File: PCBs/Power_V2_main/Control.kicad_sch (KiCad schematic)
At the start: 24 parts, among them IC1 W25Q16JVUXIQ_TR, J7 USB_C_Receptacle_USB2.0_16P, U2 ESP32-S3, U3 USBLC6-2SC6, Y1 7M40000010

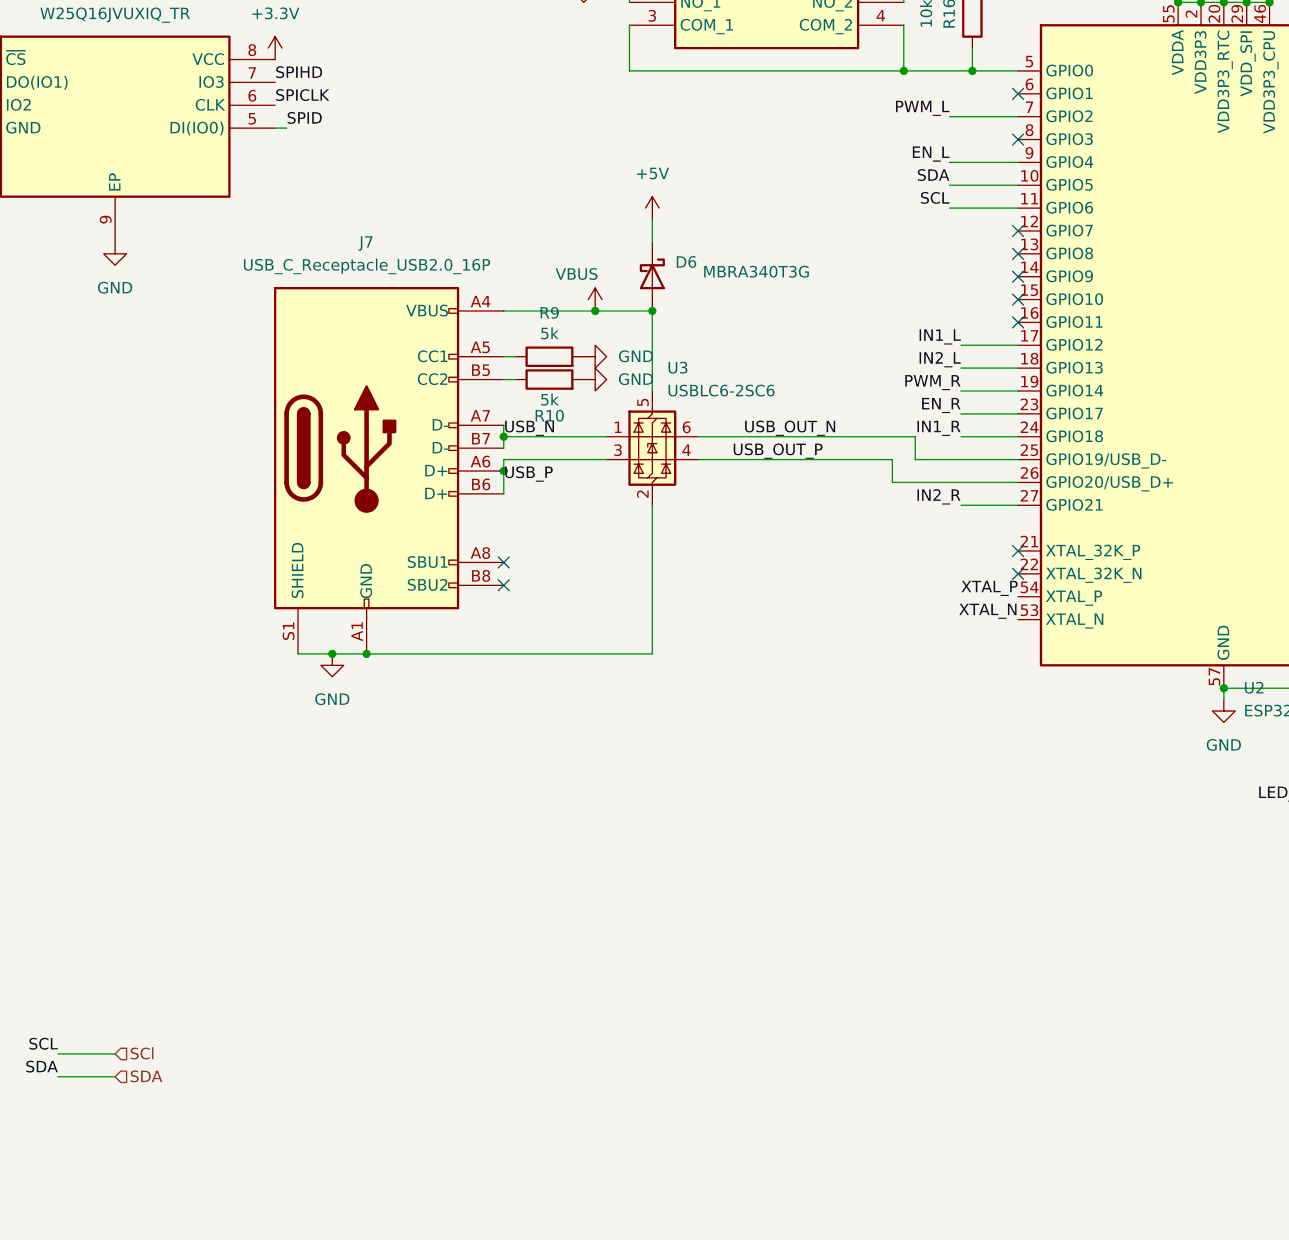
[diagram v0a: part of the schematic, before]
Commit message: shortened main board and secondary
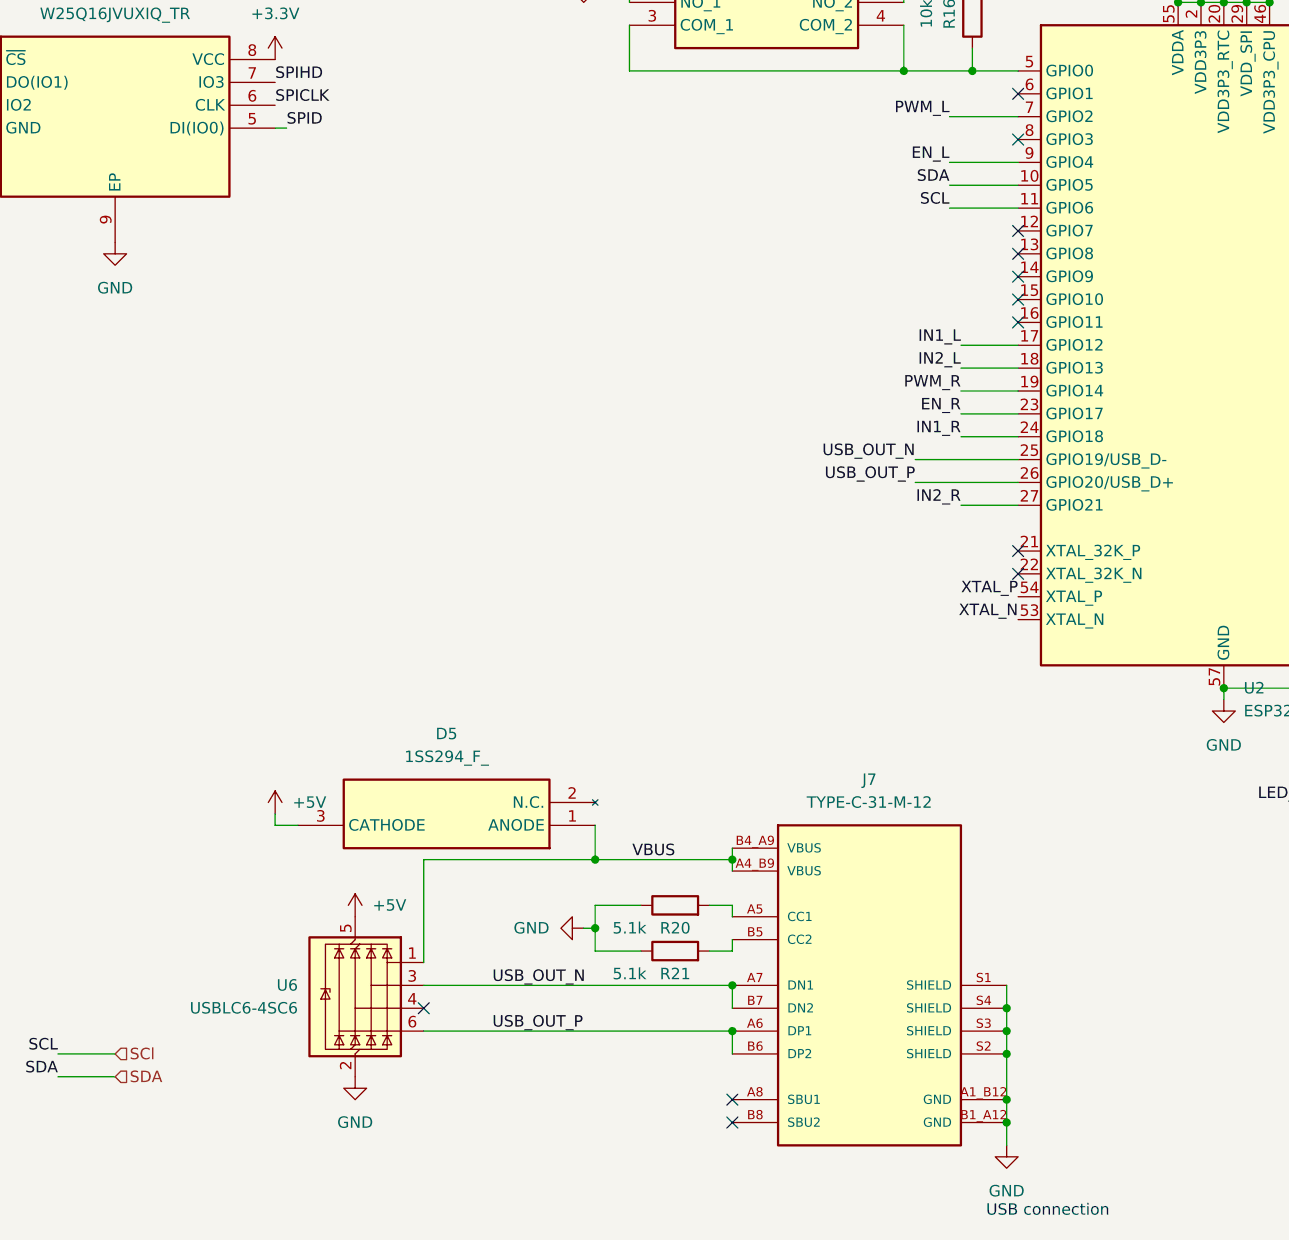
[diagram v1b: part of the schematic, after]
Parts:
- removed D6: MBRA340T3G, Diode_SMD:D_SMA, symbol Device:D_Schottky
- removed J7: USB_C_Receptacle_USB2.0_16P, IPRL_footprints:TYPE-C-31-M-12, symbol Connector:USB_C_Receptacle_USB2.0_16P
- removed R10, R9: 5k, Resistor_SMD:R_0805_2012Metric, symbol Device:R
- removed U3: USBLC6-2SC6, Package_TO_SOT_SMD:SOT-23-6, symbol Power_Protection:USBLC6-2SC6
- added D5: 1SS294_F_, iprl_footprint:SOT95P260X140-3N, symbol 1SS294_F_:1SS294_F_
- added J7: TYPE-C-31-M-12, iprl_footprints:TYPE-C-31-M-12, symbol TYPE-C-31-M-12:TYPE-C-31-M-12
- added R20, R21: 5.1k, Resistor_SMD:R_0805_2012Metric, symbol Device:R
- added U6: USBLC6-4SC6, Package_TO_SOT_SMD:SOT-23-6, symbol Power_Protection:USBLC6-4SC6
- BOOT1: footprint IPRL_footprints:PTS645SK43SMTR92LFS -> iprl_footprints:PTS645SK43SMTR92LFS
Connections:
- net +5V: now also D5.3 (CATHODE), U6.5 (VBUS)
- net GND: now also J7.A1_B12 (GND), J7.B1_A12 (GND), J7.S1 (SHIELD), J7.S2 (SHIELD), J7.S3 (SHIELD), J7.S4 (SHIELD), R20.1, R21.1, U6.2 (GND)
- net USB_OUT_N: now also J7.A7 (DN1), J7.B7 (DN2), U6.3 (I/O2)
- net USB_OUT_P: now also J7.A6 (DP1), J7.B6 (DP2), U6.6 (I/O4)
- net VBUS: now also D5.1 (ANODE), J7.A4_B9 (VBUS), J7.B4_A9 (VBUS), U6.1 (I/O1)
- new net: J7.A5 (CC1), R20.2
- new net: J7.B5 (CC2), R21.2
- no-connect marks 28 -> 29
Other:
- note added: "USB connection"

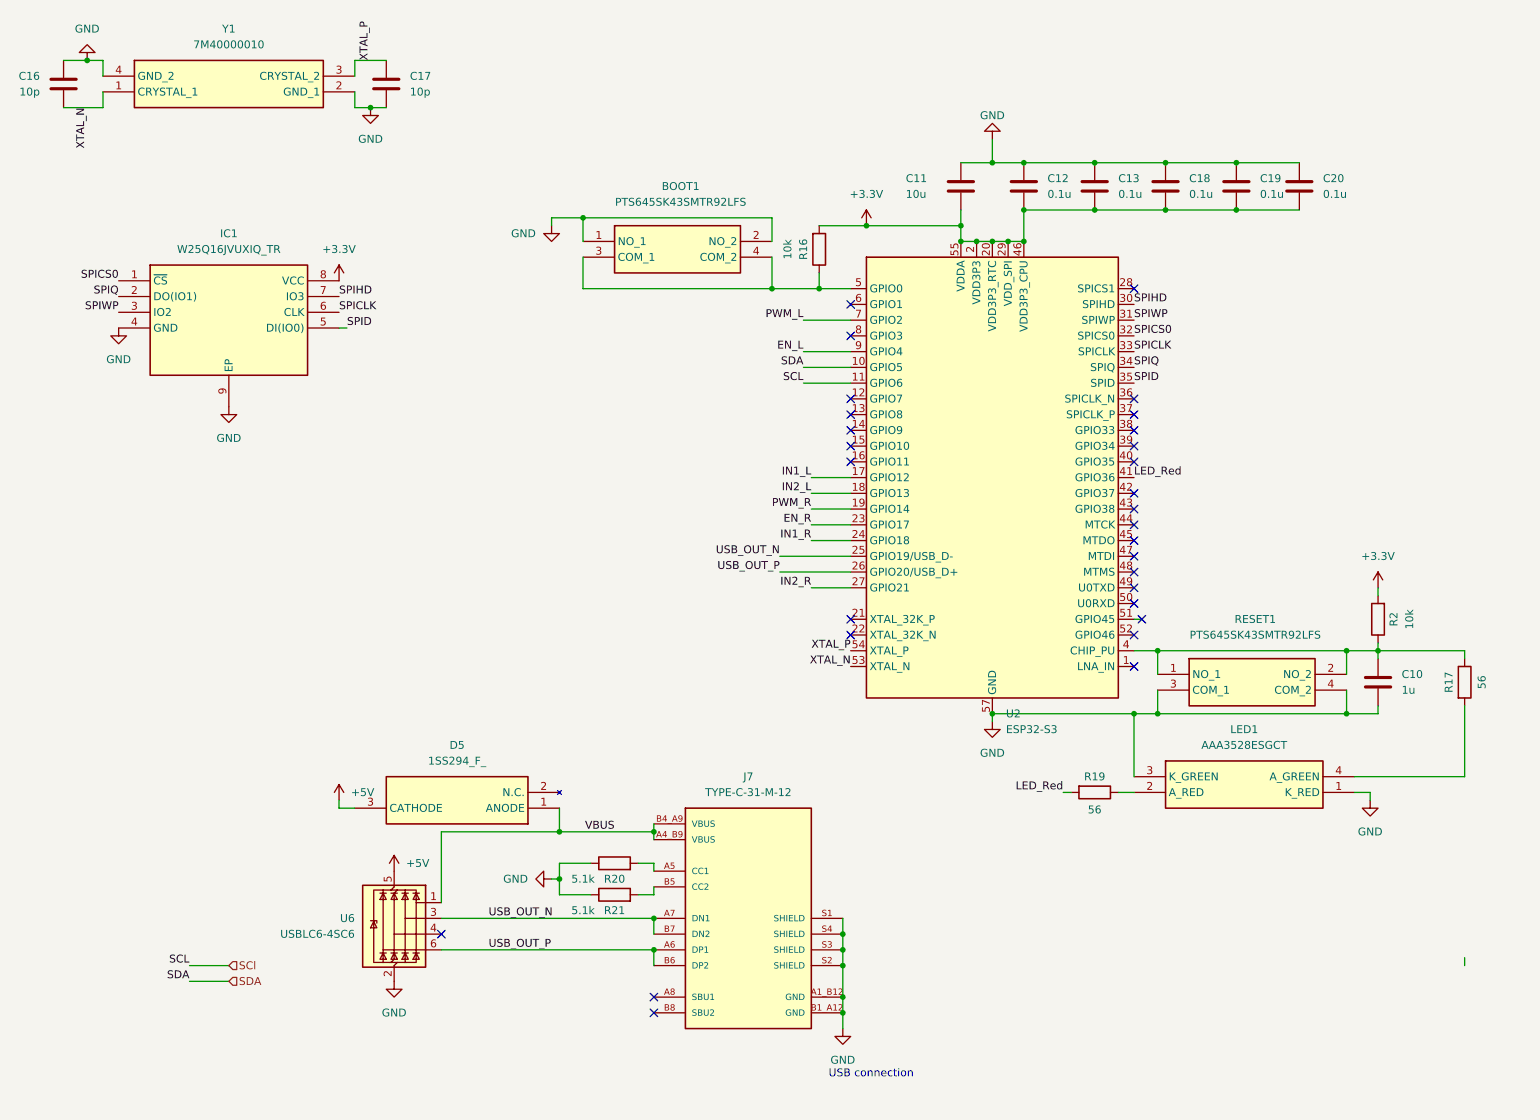
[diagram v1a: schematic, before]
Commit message: main schematic for power board main
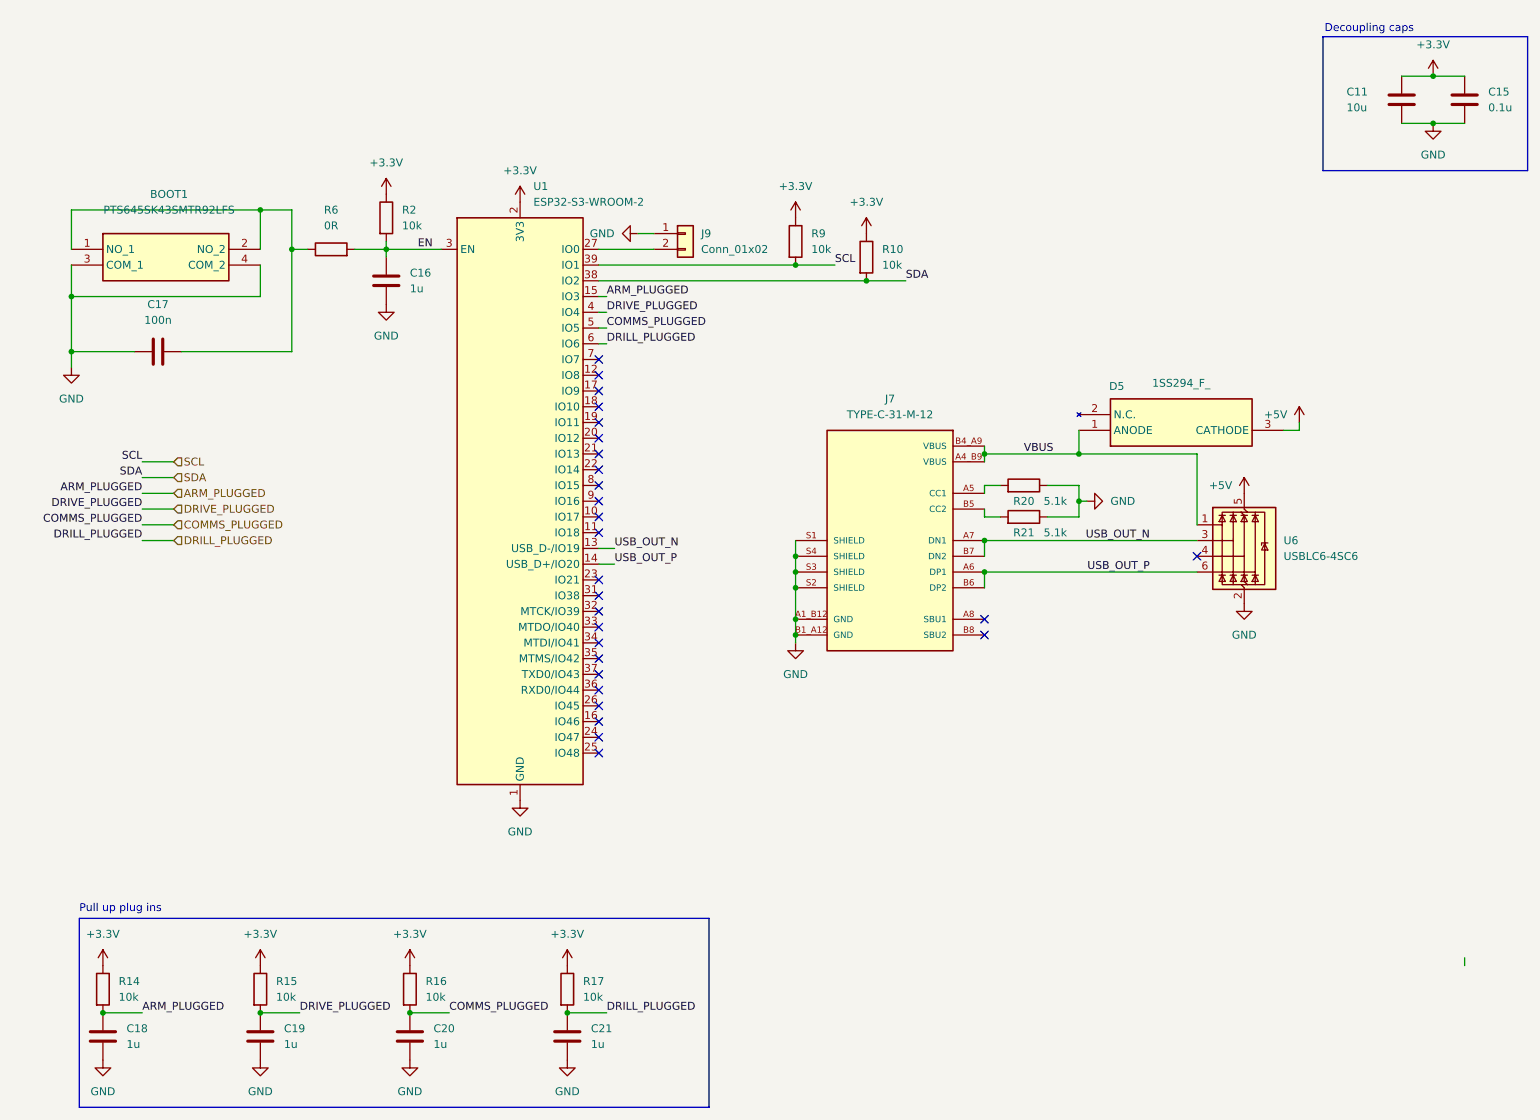
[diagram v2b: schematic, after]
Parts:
- removed C10: 1u, Capacitor_SMD:C_0603_1608Metric, symbol Device:C
- removed C12, C13: 0.1u, Capacitor_SMD:C_0603_1608Metric, symbol Device:C
- removed IC1: W25Q16JVUXIQ_TR, iprl_footprints:SON50P300X200X60-9N, symbol W25Q16JVUXIQ_TR:W25Q16JVUXIQ_TR
- removed LED1: AAA3528ESGCT, iprl_footprints:AAA3528ESGCT, symbol AAA3528ESGCT:AAA3528ESGCT
- removed R19: 56, Resistor_SMD:R_0805_2012Metric, symbol Device:R
- removed RESET1: PTS645SK43SMTR92LFS, IPRL_footprints:PTS645SK43SMTR92LFS, symbol PTS645SK43SMTR92LFS:PTS645SK43SMTR92LFS
- removed U2: ESP32-S3, Package_DFN_QFN:QFN-56-1EP_7x7mm_P0.4mm_EP4x4mm, symbol MCU_Espressif:ESP32-S3
- removed Y1: 7M40000010, iprl_footprints:7M40000010, symbol 7M40000010:7M40000010
- added C15: 0.1u, Capacitor_SMD:C_0805_2012Metric, symbol Device:C
- added C21: 1u, Capacitor_SMD:C_0805_2012Metric, symbol Device:C
- added J9: Conn_01x02, Connector_PinHeader_2.54mm:PinHeader_1x02_P2.54mm_Vertical, symbol Connector_Generic:Conn_01x02
- added R10, R14, R15, R9: 10k, Resistor_SMD:R_0805_2012Metric, symbol Device:R
- added R6: 0R, Resistor_SMD:R_0805_2012Metric, symbol Device:R
- added U1: ESP32-S3-WROOM-2, RF_Module:ESP32-S3-WROOM-2, symbol RF_Module:ESP32-S3-WROOM-2
- C11: footprint Capacitor_SMD:C_0603_1608Metric -> Capacitor_SMD:C_0805_2012Metric
- C16: value 10p -> 1u; footprint Capacitor_SMD:C_0603_1608Metric -> Capacitor_SMD:C_0805_2012Metric
- C17: value 10p -> 100n; footprint Capacitor_SMD:C_0603_1608Metric -> Capacitor_SMD:C_0805_2012Metric
- C18, C19, C20: value 0.1u -> 1u; footprint Capacitor_SMD:C_0603_1608Metric -> Capacitor_SMD:C_0805_2012Metric
- R17: value 56 -> 10k
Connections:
- net XTAL_N is gone; now on net GND: C16.2
- net XTAL_P is gone; now on net GND: C17.1
- net +3.3V: now also C11.1, R16.1, R17.1, R2.1, C15.1, R10.1, R14.1, R15.1, R9.1, U1.2 (3V3); no longer C11.2, C18.2, C19.2, C20.2, R16.2, R2.2
- net GND: now also BOOT1.3 (COM_1), BOOT1.4 (COM_2), C11.2, C18.2, C19.2, C20.2, C15.2, C21.2, J9.1 (Pin_1), U1.1 (GND), U1.40 (GND), U1.41 (GND); no longer BOOT1.1 (NO_1), BOOT1.2 (NO_2), C11.1, C16.1, C17.2, C18.1, C19.1, C20.1
- net SDA: now also R10.2, U1.38 (IO2)
- net USB_OUT_N: now also U1.13 (USB_D-/IO19)
- net USB_OUT_P: now also U1.14 (USB_D+/IO20)
- net DRILL_PLUGGED: now reaches R17.2
- net DRILL_PLUGGED: now also C21.1, U1.6 (IO6)
- new net: J9.2 (Pin_2), U1.27 (IO0)
- new net: BOOT1.1 (NO_1), BOOT1.2 (NO_2), C17.2, R6.1
- new net ARM_PLUGGED: C18.1, R14.2, U1.15 (IO3)
- new net COMMS_PLUGGED: C20.1, R16.2, U1.5 (IO5)
- new net DRIVE_PLUGGED: C19.1, R15.2, U1.4 (IO4)
- new net EN: C16.1, R2.2, R6.2, U1.3 (EN)
- new net SCL: R9.2, U1.39 (IO1)
- no-connect marks 29 -> 27
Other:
- note added: "Decoupling caps"
- note added: "Pull up plug ins"
- note removed: "USB connection"
- moved on the sheet: BOOT1, C11, D5, J7, R20, R21, U6

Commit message: a 5 hour binge of PCB layout on the main
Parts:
- removed C18, C19, C20, C21: 1u, Capacitor_SMD:C_0805_2012Metric, symbol Device:C
- removed D5: 1SS294_F_, iprl_footprint:SOT95P260X140-3N, symbol 1SS294_F_:1SS294_F_
- removed R14, R15, R16, R17: 10k, Resistor_SMD:R_0805_2012Metric, symbol Device:R
- removed R6: 0R, Resistor_SMD:R_0805_2012Metric, symbol Device:R
- added D6: MBRA340T3G, Diode_SMD:D_SMA, symbol Device:D_Schottky
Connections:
- net +5V: now also D6.1 (K)
- net EN: now also BOOT1.1 (NO_1), BOOT1.2 (NO_2), C17.2
- net VBUS: now also D6.2 (A)
- net ARM_PLUGGED: no longer names the net of U1.15 (IO3)
- net COMMS_PLUGGED: no longer names the net of U1.5 (IO5)
- net DRILL_PLUGGED: no longer names the net of U1.6 (IO6)
- net DRIVE_PLUGGED: no longer names the net of U1.4 (IO4)
- no-connect marks 27 -> 31
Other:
- note removed: "Pull up plug ins"
